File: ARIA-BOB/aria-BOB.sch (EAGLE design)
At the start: 14 parts

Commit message: revoked changes
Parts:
- U$1: value ARIATHROUGHHOLE -> ARIA; device octanis-beat:ARIATHROUGHHOLE -> octanis-beat:ARIA
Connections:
- net USBA_N renamed USBA-
- net USBB_N renamed USBB-
- net USBC_N renamed USBC-
- net USBC_P renamed USBC+
- removed net USBA_P: U$1.E19, USBA.3
- removed net USBB_P: U$1.E16, USBB.3
- new net USBA+: U$1.E19
- new net USBB+: U$1.E16, USBA.3, USBB.3

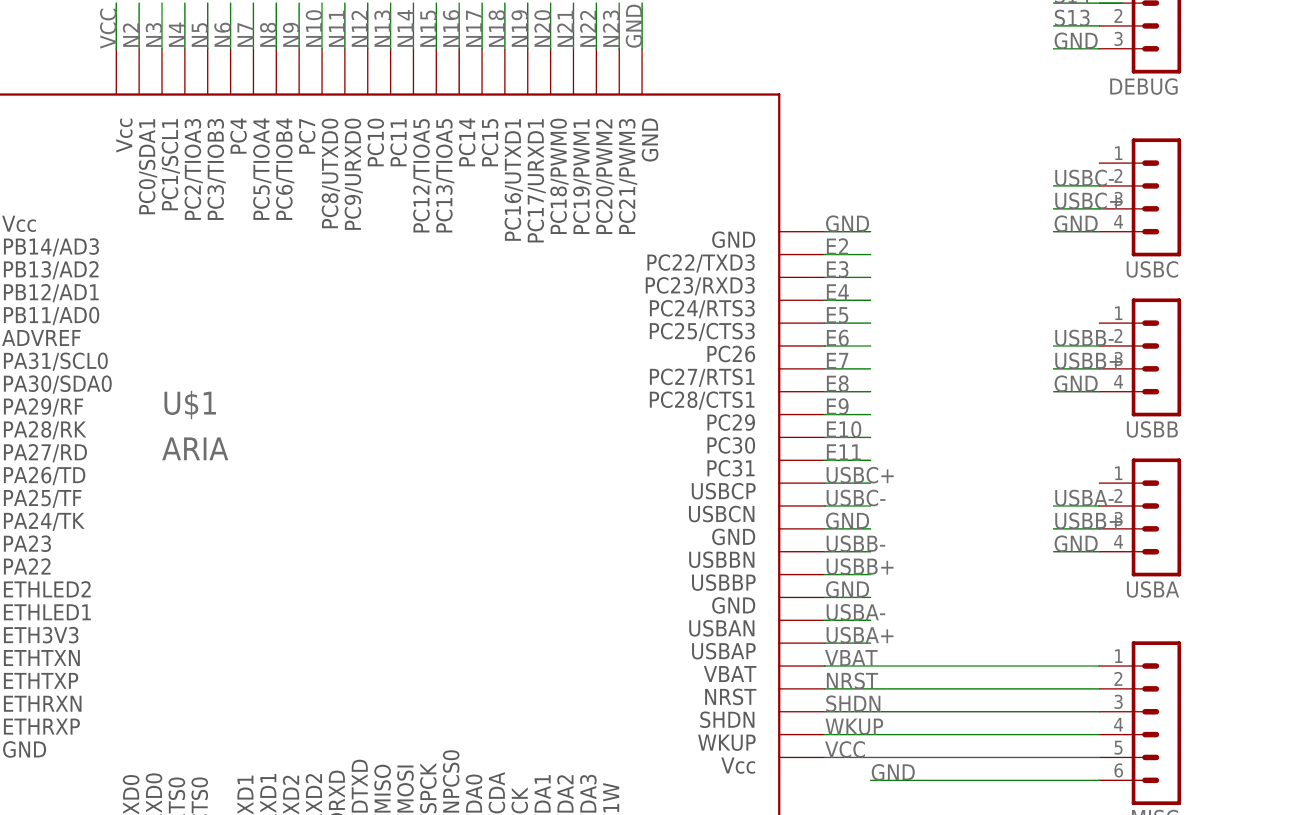
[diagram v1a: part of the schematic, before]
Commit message: changed to throughhole
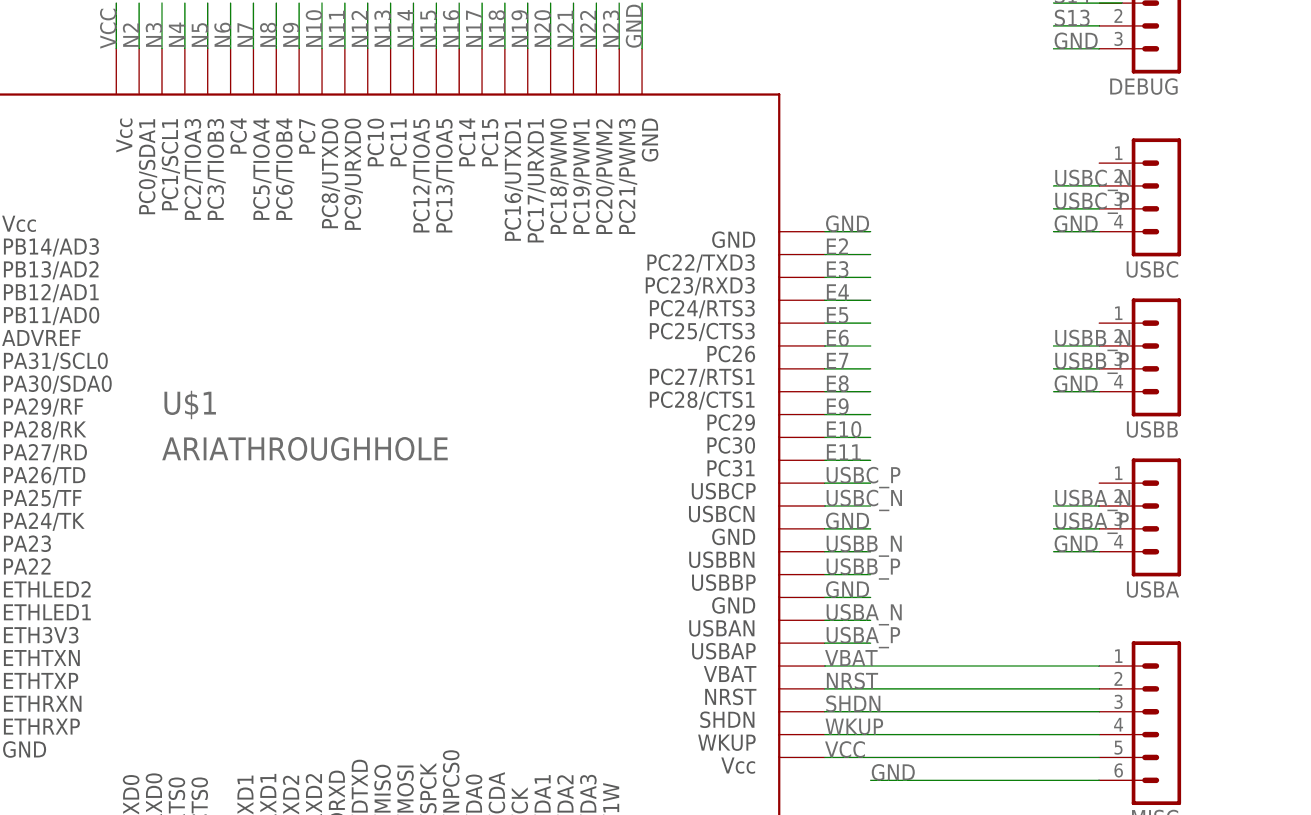
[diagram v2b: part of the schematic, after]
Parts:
- U$1: value ARIA -> ARIATHROUGHHOLE; device octanis-beat:ARIA -> octanis-beat:ARIATHROUGHHOLE
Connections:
- net USBA- renamed USBA_N
- net USBB- renamed USBB_N
- net USBC+ renamed USBC_P
- net USBC- renamed USBC_N
- removed net USBA+: U$1.E19
- removed net USBB+: U$1.E16, USBA.3, USBB.3
- new net USBA_P: U$1.E19, USBA.3
- new net USBB_P: U$1.E16, USBB.3
